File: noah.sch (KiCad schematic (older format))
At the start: 139 parts, among them U1 ATmega32U4-AU, U2 SRV05-4

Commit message: update BOM
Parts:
- D1, D10, D11, D12, D13, D14, D15, D17, D18, D19, D2, D20, D21, D22, D23, D24, D25, D26, D27, D28, D29, D3, D30, D32, D33, D35, D36, D4, D5, D6, D7, D8, D9: LCSC C8553 -> C68978
- R4: value 470 -> 1k; LCSC C17710 -> C17513
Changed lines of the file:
@@
 P 4300 9150
 F 0 "R4" V 4104 9150 50  0000 C CNN
-F 1 "470" V 4195 9150 50  0000 C CNN
+F 1 "1k" V 4195 9150 50  0000 C CNN
 F 2 "Resistor_SMD:R_0805_2012Metric" H 4300 9150 50  0001 C CNN
 F 3 "~" H 4300 9150 50  0001 C CNN
-F 4 "C17710" V 4300 9150 50  0001 C CNN "LCSC"
+F 4 "C17513" V 4300 9150 50  0001 C CNN "LCSC"
 	1    4300 9150
 	0    1    1    0
@@
 F 2 "custom_parts:D_SOT-23_ANK" V 7200 2900 50  0001 C CNN
 F 3 "~" V 7200 2900 50  0001 C CNN
-F 4 "C8553" H 7200 2900 50  0001 C CNN "LCSC"
+F 4 "C68978" H 7200 2900 50  0001 C CNN "LCSC"
 	1    7200 2900
 	0    -1   -1   0
@@
 F 2 "custom_parts:D_SOT-23_ANK" V 8100 2900 50  0001 C CNN
 F 3 "~" V 8100 2900 50  0001 C CNN
-F 4 "C8553" H 8100 2900 50  0001 C CNN "LCSC"
+F 4 "C68978" H 8100 2900 50  0001 C CNN "LCSC"
 	1    8100 2900
 	0    -1   -1   0
@@
 F 2 "custom_parts:D_SOT-23_ANK" V 9000 2900 50  0001 C CNN
 F 3 "~" V 9000 2900 50  0001 C CNN
-F 4 "C8553" H 9000 2900 50  0001 C CNN "LCSC"
+F 4 "C68978" H 9000 2900 50  0001 C CNN "LCSC"
 	1    9000 2900
 	0    -1   -1   0
@@
 F 2 "custom_parts:D_SOT-23_ANK" V 9900 2900 50  0001 C CNN
 F 3 "~" V 9900 2900 50  0001 C CNN
-F 4 "C8553" H 9900 2900 50  0001 C CNN "LCSC"
+F 4 "C68978" H 9900 2900 50  0001 C CNN "LCSC"
 	1    9900 2900
 	0    -1   -1   0
@@
 F 2 "custom_parts:D_SOT-23_ANK" V 10800 2900 50  0001 C CNN
 F 3 "~" V 10800 2900 50  0001 C CNN
-F 4 "C8553" H 10800 2900 50  0001 C CNN "LCSC"
+F 4 "C68978" H 10800 2900 50  0001 C CNN "LCSC"
 	1    10800 2900
 	0    -1   -1   0
@@
 F 2 "custom_parts:D_SOT-23_ANK" V 11700 2900 50  0001 C CNN
 F 3 "~" V 11700 2900 50  0001 C CNN
-F 4 "C8553" H 11700 2900 50  0001 C CNN "LCSC"
+F 4 "C68978" H 11700 2900 50  0001 C CNN "LCSC"
 	1    11700 2900
 	0    -1   -1   0
@@
 F 2 "custom_parts:D_SOT-23_ANK" V 12600 2900 50  0001 C CNN
 F 3 "~" V 12600 2900 50  0001 C CNN
-F 4 "C8553" H 12600 2900 50  0001 C CNN "LCSC"
+F 4 "C68978" H 12600 2900 50  0001 C CNN "LCSC"
 	1    12600 2900
 	0    -1   -1   0
@@
 F 2 "custom_parts:D_SOT-23_ANK" V 7200 3550 50  0001 C CNN
 F 3 "~" V 7200 3550 50  0001 C CNN
-F 4 "C8553" H 7200 3550 50  0001 C CNN "LCSC"
+F 4 "C68978" H 7200 3550 50  0001 C CNN "LCSC"
 	1    7200 3550
 	0    -1   -1   0
@@
 F 2 "custom_parts:D_SOT-23_ANK" V 8100 3550 50  0001 C CNN
 F 3 "~" V 8100 3550 50  0001 C CNN
-F 4 "C8553" H 8100 3550 50  0001 C CNN "LCSC"
+F 4 "C68978" H 8100 3550 50  0001 C CNN "LCSC"
 	1    8100 3550
 	0    -1   -1   0
@@
 F 2 "custom_parts:D_SOT-23_ANK" V 9000 3550 50  0001 C CNN
 F 3 "~" V 9000 3550 50  0001 C CNN
-F 4 "C8553" H 9000 3550 50  0001 C CNN "LCSC"
+F 4 "C68978" H 9000 3550 50  0001 C CNN "LCSC"
 	1    9000 3550
 	0    -1   -1   0
@@
 F 2 "custom_parts:D_SOT-23_ANK" V 9900 3550 50  0001 C CNN
 F 3 "~" V 9900 3550 50  0001 C CNN
-F 4 "C8553" H 9900 3550 50  0001 C CNN "LCSC"
+F 4 "C68978" H 9900 3550 50  0001 C CNN "LCSC"
 	1    9900 3550
 	0    -1   -1   0
@@
 F 2 "custom_parts:D_SOT-23_ANK" V 10800 3550 50  0001 C CNN
 F 3 "~" V 10800 3550 50  0001 C CNN
-F 4 "C8553" H 10800 3550 50  0001 C CNN "LCSC"
+F 4 "C68978" H 10800 3550 50  0001 C CNN "LCSC"
 	1    10800 3550
 	0    -1   -1   0
@@
 F 2 "custom_parts:D_SOT-23_ANK" V 11700 3550 50  0001 C CNN
 F 3 "~" V 11700 3550 50  0001 C CNN
-F 4 "C8553" H 11700 3550 50  0001 C CNN "LCSC"
+F 4 "C68978" H 11700 3550 50  0001 C CNN "LCSC"
 	1    11700 3550
 	0    -1   -1   0
@@
 F 2 "custom_parts:D_SOT-23_ANK" V 12600 3550 50  0001 C CNN
 F 3 "~" V 12600 3550 50  0001 C CNN
-F 4 "C8553" H 12600 3550 50  0001 C CNN "LCSC"
+F 4 "C68978" H 12600 3550 50  0001 C CNN "LCSC"
 	1    12600 3550
 	0    -1   -1   0
@@
 F 2 "custom_parts:D_SOT-23_ANK" V 7200 4200 50  0001 C CNN
 F 3 "~" V 7200 4200 50  0001 C CNN
-F 4 "C8553" H 7200 4200 50  0001 C CNN "LCSC"
+F 4 "C68978" H 7200 4200 50  0001 C CNN "LCSC"
 	1    7200 4200
 	0    -1   -1   0
@@
 F 2 "custom_parts:D_SOT-23_ANK" V 8100 4200 50  0001 C CNN
 F 3 "~" V 8100 4200 50  0001 C CNN
-F 4 "C8553" H 8100 4200 50  0001 C CNN "LCSC"
+F 4 "C68978" H 8100 4200 50  0001 C CNN "LCSC"
 	1    8100 4200
 	0    -1   -1   0
@@
 F 2 "custom_parts:D_SOT-23_ANK" V 9000 4200 50  0001 C CNN
 F 3 "~" V 9000 4200 50  0001 C CNN
-F 4 "C8553" H 9000 4200 50  0001 C CNN "LCSC"
+F 4 "C68978" H 9000 4200 50  0001 C CNN "LCSC"
 	1    9000 4200
 	0    -1   -1   0
@@
 F 2 "custom_parts:D_SOT-23_ANK" V 9900 4200 50  0001 C CNN
 F 3 "~" V 9900 4200 50  0001 C CNN
-F 4 "C8553" H 9900 4200 50  0001 C CNN "LCSC"
+F 4 "C68978" H 9900 4200 50  0001 C CNN "LCSC"
 	1    9900 4200
 	0    -1   -1   0
@@
 F 2 "custom_parts:D_SOT-23_ANK" V 10800 4200 50  0001 C CNN
 F 3 "~" V 10800 4200 50  0001 C CNN
-F 4 "C8553" H 10800 4200 50  0001 C CNN "LCSC"
+F 4 "C68978" H 10800 4200 50  0001 C CNN "LCSC"
 	1    10800 4200
 	0    -1   -1   0
@@
 F 2 "custom_parts:D_SOT-23_ANK" V 11700 4200 50  0001 C CNN
 F 3 "~" V 11700 4200 50  0001 C CNN
-F 4 "C8553" H 11700 4200 50  0001 C CNN "LCSC"
+F 4 "C68978" H 11700 4200 50  0001 C CNN "LCSC"
 	1    11700 4200
 	0    -1   -1   0
@@
 F 2 "custom_parts:D_SOT-23_ANK" V 7200 4850 50  0001 C CNN
 F 3 "~" V 7200 4850 50  0001 C CNN
-F 4 "C8553" H 7200 4850 50  0001 C CNN "LCSC"
+F 4 "C68978" H 7200 4850 50  0001 C CNN "LCSC"
 	1    7200 4850
 	0    -1   -1   0
@@
 F 2 "custom_parts:D_SOT-23_ANK" V 8100 4850 50  0001 C CNN
 F 3 "~" V 8100 4850 50  0001 C CNN
-F 4 "C8553" H 8100 4850 50  0001 C CNN "LCSC"
+F 4 "C68978" H 8100 4850 50  0001 C CNN "LCSC"
 	1    8100 4850
 	0    -1   -1   0
@@
 F 2 "custom_parts:D_SOT-23_ANK" V 9000 4850 50  0001 C CNN
 F 3 "~" V 9000 4850 50  0001 C CNN
-F 4 "C8553" H 9000 4850 50  0001 C CNN "LCSC"
+F 4 "C68978" H 9000 4850 50  0001 C CNN "LCSC"
 	1    9000 4850
 	0    -1   -1   0
@@
 F 2 "custom_parts:D_SOT-23_ANK" V 9900 4850 50  0001 C CNN
 F 3 "~" V 9900 4850 50  0001 C CNN
-F 4 "C8553" H 9900 4850 50  0001 C CNN "LCSC"
+F 4 "C68978" H 9900 4850 50  0001 C CNN "LCSC"
 	1    9900 4850
 	0    -1   -1   0
@@
 F 2 "custom_parts:D_SOT-23_ANK" V 10800 4850 50  0001 C CNN
 F 3 "~" V 10800 4850 50  0001 C CNN
-F 4 "C8553" H 10800 4850 50  0001 C CNN "LCSC"
+F 4 "C68978" H 10800 4850 50  0001 C CNN "LCSC"
 	1    10800 4850
 	0    -1   -1   0
@@
 F 2 "custom_parts:D_SOT-23_ANK" V 11700 4850 50  0001 C CNN
 F 3 "~" V 11700 4850 50  0001 C CNN
-F 4 "C8553" H 11700 4850 50  0001 C CNN "LCSC"
+F 4 "C68978" H 11700 4850 50  0001 C CNN "LCSC"
 	1    11700 4850
 	0    -1   -1   0
@@
 F 2 "custom_parts:D_SOT-23_ANK" V 12600 4850 50  0001 C CNN
 F 3 "~" V 12600 4850 50  0001 C CNN
-F 4 "C8553" H 12600 4850 50  0001 C CNN "LCSC"
+F 4 "C68978" H 12600 4850 50  0001 C CNN "LCSC"
 	1    12600 4850
 	0    -1   -1   0
@@
 F 2 "custom_parts:D_SOT-23_ANK" V 7200 5500 50  0001 C CNN
 F 3 "~" V 7200 5500 50  0001 C CNN
-F 4 "C8553" H 7200 5500 50  0001 C CNN "LCSC"
+F 4 "C68978" H 7200 5500 50  0001 C CNN "LCSC"
 	1    7200 5500
 	0    -1   -1   0
@@
 F 2 "custom_parts:D_SOT-23_ANK" V 8100 5500 50  0001 C CNN
 F 3 "~" V 8100 5500 50  0001 C CNN
-F 4 "C8553" H 8100 5500 50  0001 C CNN "LCSC"
+F 4 "C68978" H 8100 5500 50  0001 C CNN "LCSC"
 	1    8100 5500
 	0    -1   -1   0
@@
 F 2 "custom_parts:D_SOT-23_ANK" V 12600 5500 50  0001 C CNN
 F 3 "~" V 12600 5500 50  0001 C CNN
-F 4 "C8553" H 12600 5500 50  0001 C CNN "LCSC"
+F 4 "C68978" H 12600 5500 50  0001 C CNN "LCSC"
 	1    12600 5500
 	0    -1   -1   0
@@
 F 2 "custom_parts:D_SOT-23_ANK" V 13500 2900 50  0001 C CNN
 F 3 "~" V 13500 2900 50  0001 C CNN
-F 4 "C8553" H 13500 2900 50  0001 C CNN "LCSC"
+F 4 "C68978" H 13500 2900 50  0001 C CNN "LCSC"
 	1    13500 2900
 	0    -1   -1   0
@@
 F 2 "custom_parts:D_SOT-23_ANK" V 13500 4200 50  0001 C CNN
 F 3 "~" V 13500 4200 50  0001 C CNN
-F 4 "C8553" H 13500 4200 50  0001 C CNN "LCSC"
+F 4 "C68978" H 13500 4200 50  0001 C CNN "LCSC"
 	1    13500 4200
 	0    -1   -1   0
@@
 F 2 "custom_parts:D_SOT-23_ANK" V 13500 5500 50  0001 C CNN
 F 3 "~" V 13500 5500 50  0001 C CNN
-F 4 "C8553" H 13500 5500 50  0001 C CNN "LCSC"
+F 4 "C68978" H 13500 5500 50  0001 C CNN "LCSC"
 	1    13500 5500
 	0    -1   -1   0

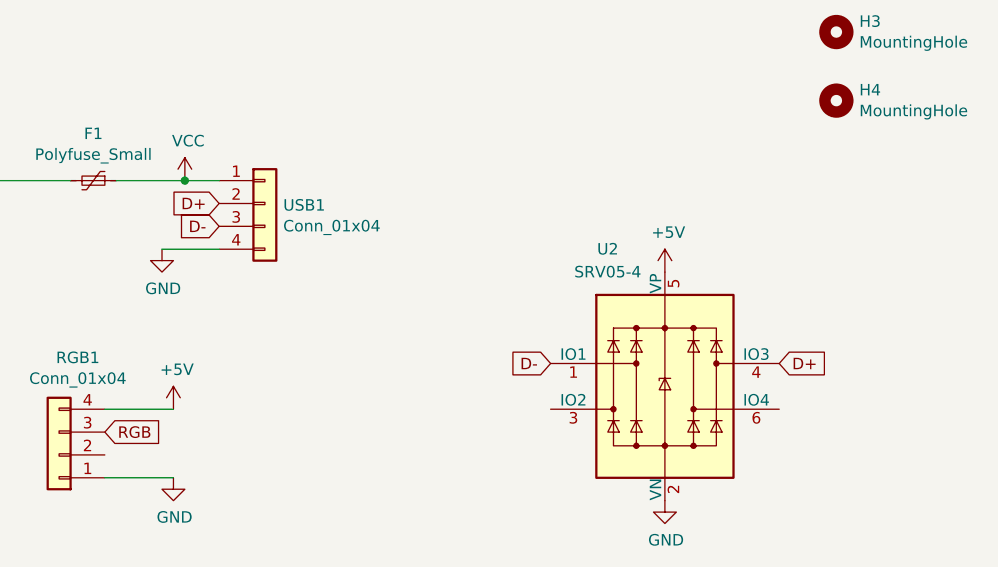
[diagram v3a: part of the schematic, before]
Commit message: fix DB plug wire orientation
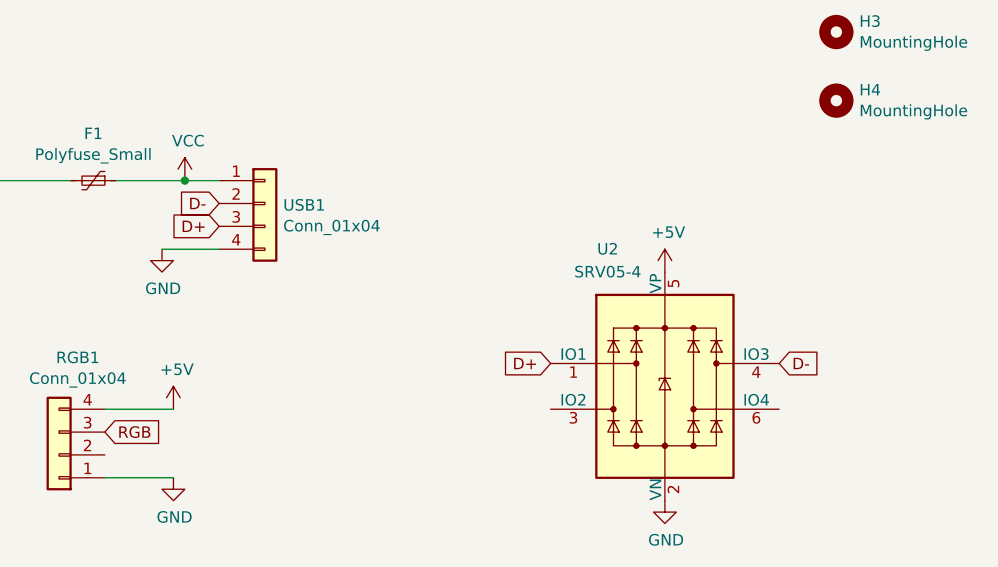
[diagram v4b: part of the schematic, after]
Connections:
- net D+: now also U2.1 (IO1), USB1.3 (Pin_3); no longer U2.4 (IO3), USB1.2 (Pin_2)
- net D-: now also U2.4 (IO3), USB1.2 (Pin_2); no longer U2.1 (IO1), USB1.3 (Pin_3)
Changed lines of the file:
@@
 Text GLabel 1450 8350 0    50   Input ~ 0
 D+
+Text GLabel 7250 8500 0    50   Input ~ 0
+D+
 Text GLabel 7250 8400 0    50   Input ~ 0
-D+
-Text GLabel 7250 8500 0    50   Input ~ 0
 D-
 $Comp
@@
 	1    0    0    -1
 $EndComp
+Text GLabel 9700 9100 2    50   Input ~ 0
+D-
 Text GLabel 8700 9100 0    50   Input ~ 0
-D-
-Text GLabel 9700 9100 2    50   Input ~ 0
 D+
 Wire Wire Line
